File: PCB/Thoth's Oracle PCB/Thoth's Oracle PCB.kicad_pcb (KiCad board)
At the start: 2 copper layers, 58.2 x 75 mm, 13 parts, among them J1 IO, J2 MCUDisplay, J3 Display, SW1 Orientation, SW2 Prev, SW3 Play/Pause, SW4 Next, SW5 RotaryEncoder_Switch

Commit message: Preparing for release
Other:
- board text added: "Thoth's Oracle PCB v1.0.0 Copyright (C) Dominique Negm 2025"
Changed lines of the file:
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@@
+		)
+	)
+	(gr_text "Thoth's Oracle PCB v1.0.0\nCopyright (C) Dominique Negm 2025"
+		(at 217.46 80.09 0)
+		(layer "B.SilkS")
+		(effects
+			(font
+				(size 1 1)
+				(thickness 0.1)
+			)
+			(justify left bottom mirror)
 		)
 	)

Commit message: Cleaned board
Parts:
- removed the REF** at (167.9, 37.5)
- J3: footprint Connector_PinSocket_2.54mm:PinSocket_1x08_P2.54mm_Vertical -> Connector_PinSocket_2.54mm:PinSocket_1x08_P2.54mm_Horizontal
- moved J3 17.8 mm to (164.1, 43.0), turned to -90 degrees
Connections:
- J3 pad 1: LED -> +5V
- J3 pad 2: P11 -> GND
- J3 pad 3: P10 -> P13
- J3 pad 4: P9 -> P12
- J3 pad 5: P12 -> P9
- J3 pad 6: P13 -> P10
- J3 pad 7: GND -> P11
- J3 pad 8: +5V -> LED
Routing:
- net +5V: track 64.7 -> 67.7 mm
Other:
- board text added: "Thoth's Oracle PCB v1.0.1 Copyright (C) Dominique Negm 2025"
- board text removed: "Thoth's Oracle PCB v1.0.0 Copyright (C) Dominique Negm 2025"

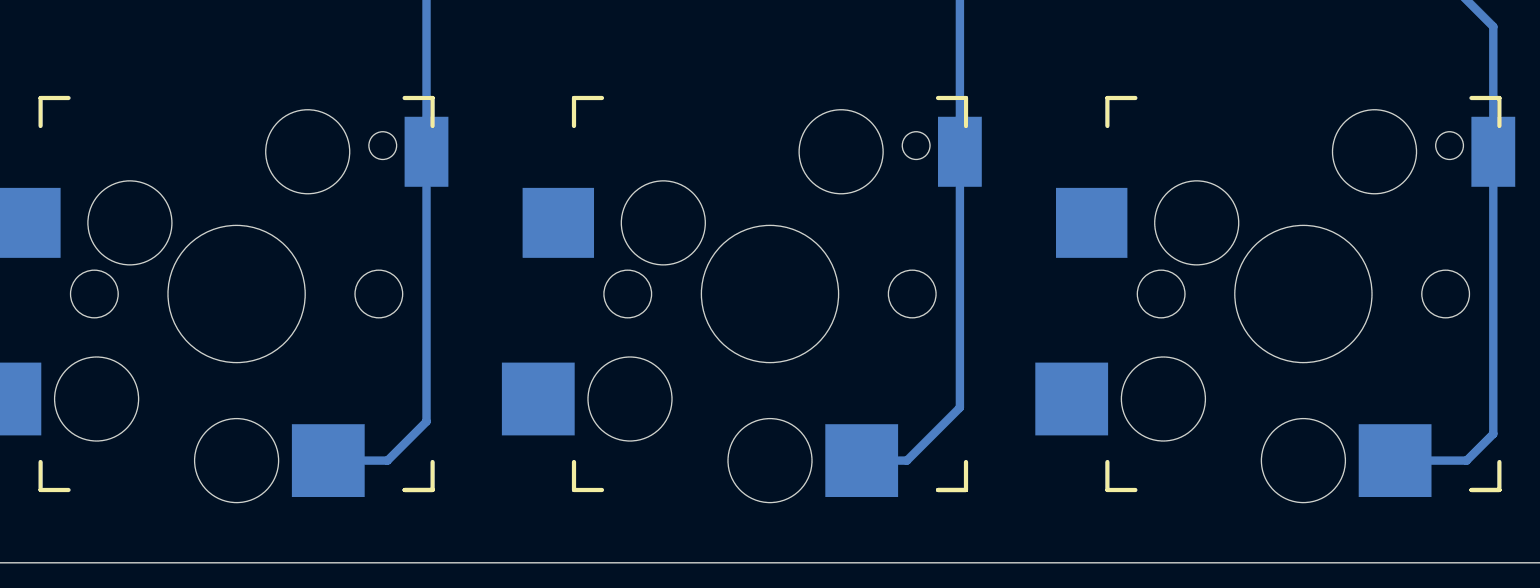
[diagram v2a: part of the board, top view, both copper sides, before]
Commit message: Separated hotswap sockets with modified footprints so they don't overlap. Typo in assembly
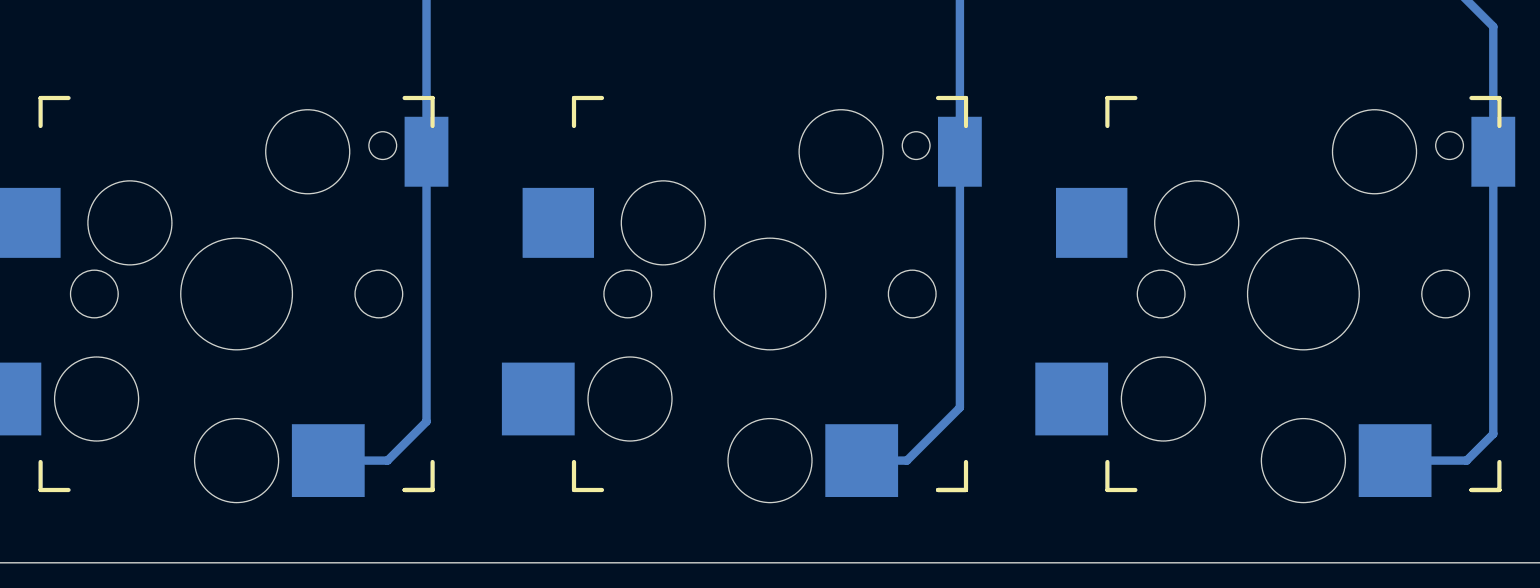
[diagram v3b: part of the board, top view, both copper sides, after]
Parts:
- added SW6: PP_Alt, keyswitches:Kailh_socket_PG1350_modified, F.Cu at (190.9, 97.4)
- added SW7: Prev_Alt, keyswitches:Kailh_socket_PG1350_modified, F.Cu at (171.9, 97.4)
- added SW8: Next_Alt, keyswitches:Kailh_socket_PG1350_modified, F.Cu at (210.0, 97.4)
- SW2, SW3, SW4: footprint keyswitches:Kailh_socket_MX_PG1350 -> keyswitches:Kailh_socket_MX_modified

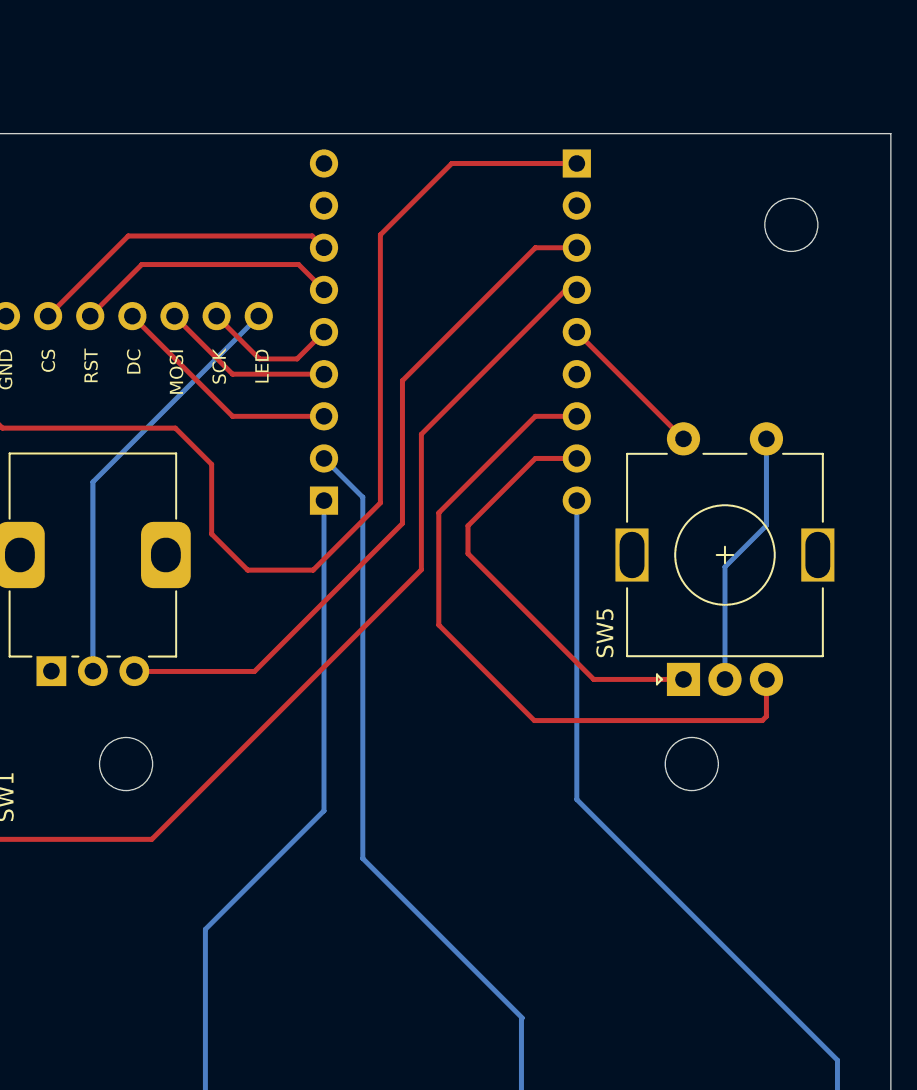
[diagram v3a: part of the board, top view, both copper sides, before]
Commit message: Working on gif capabilites with 8-bit parallel display instead of SPI
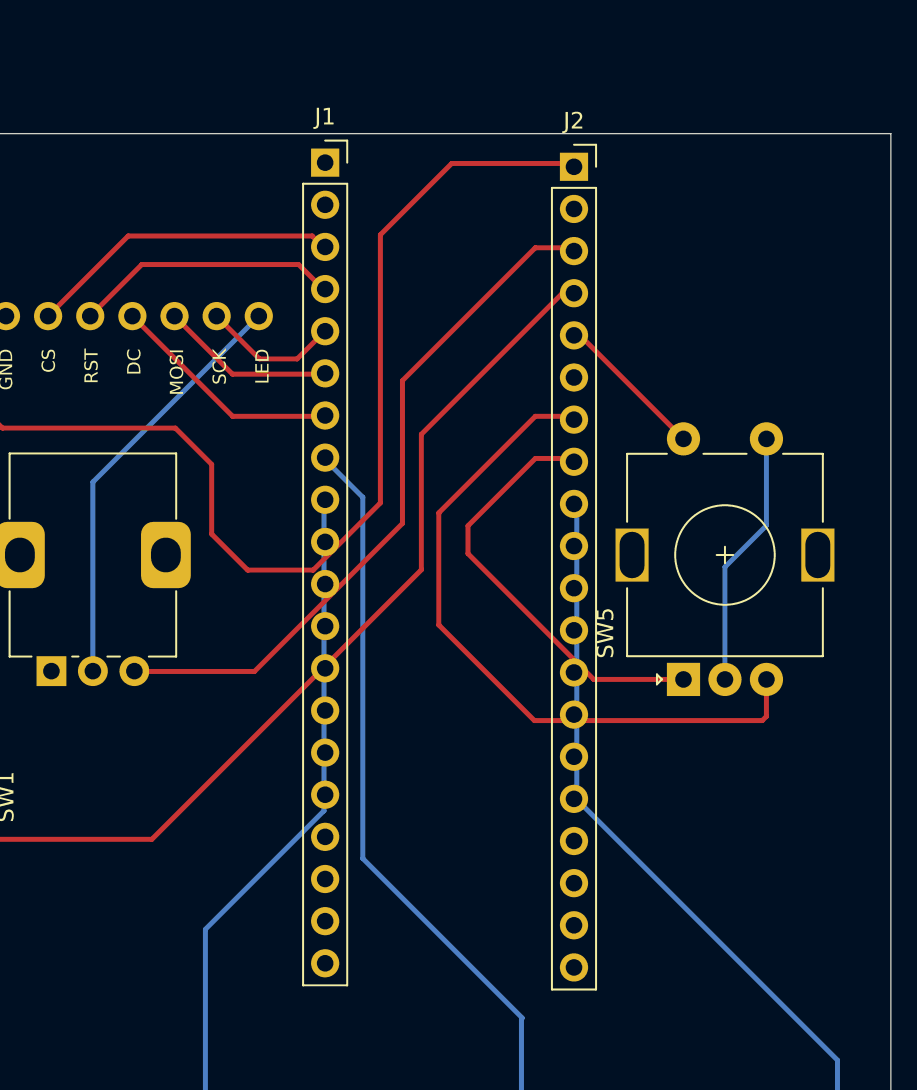
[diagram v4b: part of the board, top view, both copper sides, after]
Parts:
- removed REF** (x3): MountingHole_3.2mm_M3, MountingHole:MountingHole_3.2mm_M3
- J1: value IO -> Nano_5v; footprint Connector_PinSocket_2.54mm:PinSocket_1x09_P2.54mm_Vertical -> Connector_PinSocket_2.54mm:PinSocket_1x20_P2.54mm_Vertical; moved to F.Cu
- J2: value MCUDisplay -> Nano_3v3; footprint Connector_PinSocket_2.54mm:PinSocket_1x09_P2.54mm_Vertical -> Connector_PinSocket_2.54mm:PinSocket_1x20_P2.54mm_Vertical; moved to F.Cu
- moved J1 20.4 mm to (185.9, 33.8)
- moved J2 0.26 mm to (200.9, 34.0), turned to 0 degrees
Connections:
- J1 pad 1: P7 -> P6
- J1 pad 2: P8 -> P5
- J1 pad 3: P9 -> P2
- J1 pad 4: P10 -> P3
- J1 pad 5: P11 -> P2
- J1 pad 6: P12 -> P1
- J1 pad 7: P13 -> 3v3
- J1 pad 8: RX -> GND
- J1 pad 9: TX -> unconnected-(J1-Pin_9-Pad9)
- J2 pad 1: +5V -> P7
- J2 pad 2: GND -> P8
- J2 pad 3: 3v3 -> P9
- J2 pad 4: P1 -> P10
- J2 pad 5: P2 -> P11
- J2 pad 6: P3 -> P12
- J2 pad 7: P4 -> P13
- J2 pad 8: P5 -> RX
- J2 pad 9: P6 -> unconnected-(J2-Pin_9-Pad9)
- SW5 pad B: P4 -> unconnected-(SW5-PadB)
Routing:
- net unconnected-(SW5-PadB): track 0.00 -> 42.0 mm
- net P4: track 42.0 -> 0.00 mm
